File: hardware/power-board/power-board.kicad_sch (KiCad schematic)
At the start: 25 parts, among them J1 SW_SPST, J2 Main Board, J3 DMX512 Out Jack, J4 DMX512, K1 SPST-NO, K2 SPST-NO, P1 IEC320-C14, P2 IEC320-C13, P3 IEC320-C13, U1 NUD3112DMT1G, U2 MAX3075E

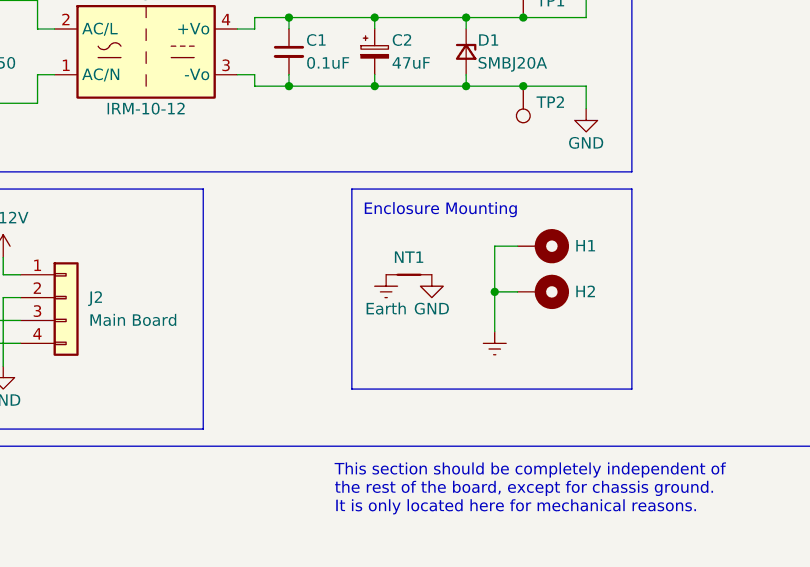
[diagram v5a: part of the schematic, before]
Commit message: Move components around for better clearance and update things
Moved the DC output filter components for better clearance
Moved one of the relays to make more space
Rerouted the relay control bits
Added a DC ground plane to make connections a bit better

Removed the net tie between DC ground and protective earth, as there's
still no good straight answer on how to do this. And they'll be
connected in other ways on the main board.
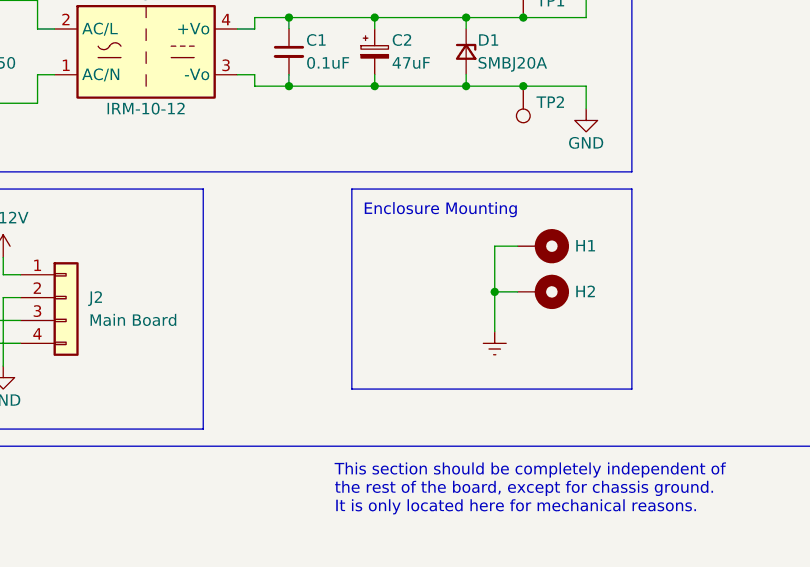
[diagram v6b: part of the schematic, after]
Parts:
- removed NT1: NetTie_2, NetTie:NetTie-2_SMD_Pad2.0mm, symbol Device:NetTie_2
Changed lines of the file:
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@@
-    )
-  )
-  (symbol (lib_id "Device:NetTie_2") (at 88.9 100.965 0) (unit 1)
-    (in_bom no) (on_board yes) (dnp no)
-    (property "Reference" "NT1" (at 88.9 99.06 0)
-      (effects (font (size 1.27 1.27)))
-    )
-    (property "Value" "NetTie_2" (at 88.9 97.79 0)
-      (effects (font (size 1.27 1.27)) hide)
-    )
-    (property "Footprint" "NetTie:NetTie-2_SMD_Pad2.0mm" (at 88.9 100.965 0)
-      (effects (font (size 1.27 1.27)) hide)
-    )
-    (property "Datasheet" "~" (at 88.9 100.965 0)
-      (effects (font (size 1.27 1.27)) hide)
-    )
-    (pin "1")
-    (pin "2")
-    (instances
-      (project "power-board"
-        (path "/31a301d9-d769-4a35-943a-fe3e3609e773"
-          (reference "NT1") (unit 1)
-        )
-      )
     )
   )
@@
     )
   )
-  (symbol (lib_id "power:GND") (at 91.44 100.965 0) (unit 1)
-    (in_bom yes) (on_board yes) (dnp no)
-    (property "Reference" "#PWR019" (at 91.44 107.315 0)
-      (effects (font (size 1.27 1.27)) hide)
-    )
-    (property "Value" "GND" (at 91.44 104.775 0)
-      (effects (font (size 1.27 1.27)))
-    )
-    (property "Footprint" "" (at 91.44 100.965 0)
-      (effects (font (size 1.27 1.27)) hide)
-    )
-    (property "Datasheet" "" (at 91.44 100.965 0)
-      (effects (font (size 1.27 1.27)) hide)
-    )
-    (pin "1")
-    (instances
-      (project "power-board"
-        (path "/31a301d9-d769-4a35-943a-fe3e3609e773"
-          (reference "#PWR019") (unit 1)
-        )
-      )
-    )
-  )
   (symbol (lib_id "Converter_ACDC:IRM-10-12") (at 59.69 76.2 0) (unit 1)
     (in_bom yes) (on_board yes) (dnp no)
@@
         )
       )
-    )
-  )
-  (symbol (lib_id "power:Earth") (at 86.36 100.965 0) (unit 1)
-    (in_bom yes) (on_board yes) (dnp no)
-    (property "Reference" "#PWR018" (at 86.36 107.315 0)
-      (effects (font (size 1.27 1.27)) hide)
-    )
-    (property "Value" "Earth" (at 86.36 104.775 0)
-      (effects (font (size 1.27 1.27)))
-    )
-    (property "Footprint" "" (at 86.36 100.965 0)
-      (effects (font (size 1.27 1.27)) hide)
-    )
-    (property "Datasheet" "~" (at 86.36 100.965 0)
-      (effects (font (size 1.27 1.27)) hide)
-    )
-    (pin "1")
-    (instances
-      (project "power-board"
-        (path "/31a301d9-d769-4a35-943a-fe3e3609e773"
-          (reference "#PWR018") (unit 1)
-        )
-      )

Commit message: Changed fuse holder from Bulgin to Schurter
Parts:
- F1: footprint Fuse:Fuseholder_Cylinder-5x20mm_Bulgin_FX0457_Horizontal_Closed -> lib_fp:Fuseholder_Cylinder-5x20mm_Schurter_FPG5_3101.0050_Horizontal_Closed; Manufacturer Bulgin -> Schurter; Manufacturer PN FX0457 -> 3101.0050; Supplier PN 708-1898-ND -> 486-1161-ND
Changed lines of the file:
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@@
       (effects (font (size 1.27 1.27)) (justify left) hide)
     )
-    (property "Footprint" "Fuse:Fuseholder_Cylinder-5x20mm_Bulgin_FX0457_Horizontal_Closed" (at 27.94 53.848 90)
+    (property "Footprint" "lib_fp:Fuseholder_Cylinder-5x20mm_Schurter_FPG5_3101.0050_Horizontal_Closed" (at 27.94 53.848 90)
       (effects (font (size 1.27 1.27)) hide)
     )
@@
       (effects (font (size 1.27 1.27)))
     )
-    (property "Description" "FUSE HLDR CARTRIDGE 250V 10A PCB" (at 27.94 52.07 0)
+    (property "Description" "FUSE HLDR CARTRIDGE 400V 16A PCB" (at 27.94 52.07 0)
       (effects (font (size 1.27 1.27)) hide)
     )
-    (property "Manufacturer" "Bulgin" (at 27.94 52.07 0)
+    (property "Manufacturer" "Schurter" (at 27.94 52.07 0)
       (effects (font (size 1.27 1.27)) hide)
     )
-    (property "Manufacturer PN" "FX0457" (at 27.94 52.07 0)
+    (property "Manufacturer PN" "3101.0050" (at 27.94 52.07 0)
       (effects (font (size 1.27 1.27)) hide)
     )
@@
       (effects (font (size 1.27 1.27)) hide)
     )
-    (property "Supplier PN" "708-1898-ND" (at 27.94 52.07 0)
+    (property "Supplier PN" "486-1161-ND" (at 27.94 52.07 0)
       (effects (font (size 1.27 1.27)) hide)
     )

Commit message: Swapped power switch connector and tweaked more power traces
Using a full receptacle and connector here takes up way too much space
and adds needless cost.  Going to instead try one of these spring
connectors that directly takes wires (with or without ferrules).
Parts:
- J1: footprint Connector_Molex:Molex_Mega-Fit_76829-0002_2x01_P5.70mm_Vertical -> lib_fp:Weidmuller_1825960000_1x02_P5.0mm; Manufacturer Molex -> Weidmüller; Manufacturer PN 0768290002 -> 1825960000; Supplier PN WM11975-ND -> 281-2124-ND
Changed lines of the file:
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@@
       (effects (font (size 1.27 1.27)) hide)
     )
-    (property "Footprint" "Connector_Molex:Molex_Mega-Fit_76829-0002_2x01_P5.70mm_Vertical" (at 41.91 52.07 0)
+    (property "Footprint" "lib_fp:Weidmuller_1825960000_1x02_P5.0mm" (at 41.91 52.07 0)
       (effects (font (size 1.27 1.27)) hide)
     )
-    (property "Datasheet" "https://www.molex.com/pdm_docs/as/AS-76823-100.pdf" (at 41.91 52.07 0)
+    (property "Datasheet" "https://media.digikey.com/pdf/Data%20Sheets/Weidmuller%20PDFs/1825960000.pdf" (at 41.91 52.07 0)
       (effects (font (size 1.27 1.27)) hide)
     )
@@
       (effects (font (size 1.27 1.27)))
     )
-    (property "Description" "CONN HEADER VERT 2POS 5.70MM" (at 41.91 52.07 0)
+    (property "Description" "TERM BLK 2POS TOP ENTRY 5MM PCB" (at 41.91 52.07 0)
       (effects (font (size 1.27 1.27)) hide)
     )
-    (property "Manufacturer" "Molex" (at 41.91 52.07 0)
+    (property "Manufacturer" "Weidmüller" (at 41.91 52.07 0)
       (effects (font (size 1.27 1.27)) hide)
     )
-    (property "Manufacturer PN" "0768290002" (at 41.91 52.07 0)
+    (property "Manufacturer PN" "1825960000" (at 41.91 52.07 0)
       (effects (font (size 1.27 1.27)) hide)
     )
@@
       (effects (font (size 1.27 1.27)) hide)
     )
-    (property "Supplier PN" "WM11975-ND" (at 41.91 52.07 0)
+    (property "Supplier PN" "281-2124-ND" (at 41.91 52.07 0)
       (effects (font (size 1.27 1.27)) hide)
     )
